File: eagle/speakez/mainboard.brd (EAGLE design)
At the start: 31 parts, among them U1 +12v

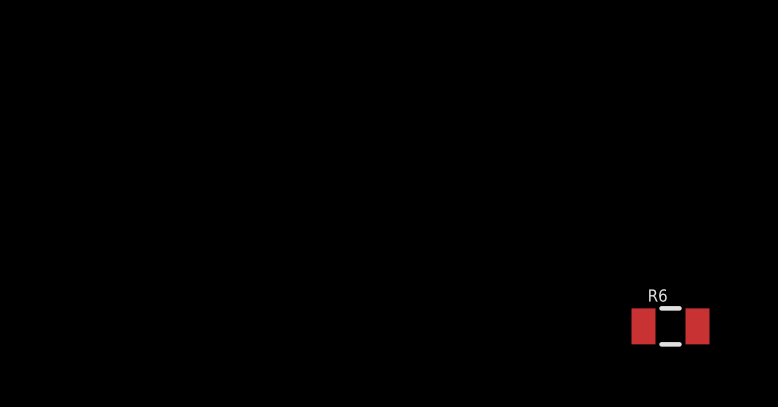
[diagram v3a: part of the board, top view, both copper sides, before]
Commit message: added decoupling caps
to microcontroller VCC pin
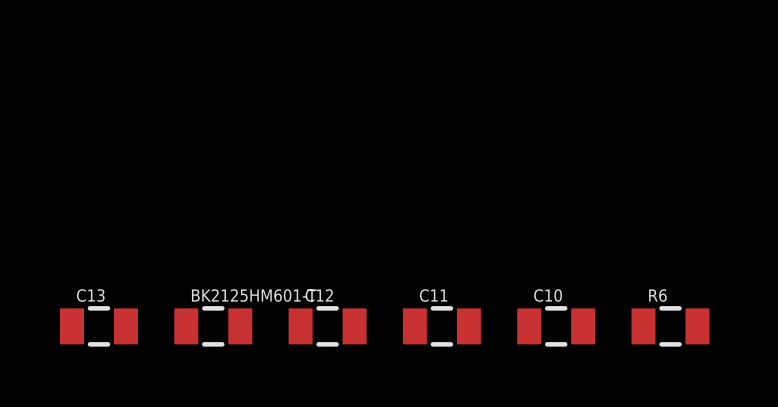
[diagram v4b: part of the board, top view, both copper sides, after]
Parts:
- added BK2125HM601-T: (no value), SparkFun-Passives:0805
- added C10, C11, C12: 0.1uF, SparkFun-Capacitors:0805
- added C13: 2.2uF, SparkFun-Capacitors:0805
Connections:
- removed net N$29: BATTERY.2, C6.2, C7.2, C8.2, PROGRAMMER-RB.1, PROGRAMMER-RB.2, PROGRAMMER-RB.3, PROGRAMMER-RB.4, PROGRAMMER-RB.5, PROGRAMMER-RT.2, PROGRAMMER-RT.3, PROGRAMMER-RT.4, PROGRAMMER-RT.5, SERIAL.4, U$1.31, U$1.4, U$1.47, U1.3
- new net N$22: BATTERY.2, C10.2, C11.2, C12.2, C13.2, C6.2, C7.2, C8.2, PROGRAMMER-RB.1, PROGRAMMER-RB.2, PROGRAMMER-RB.3, PROGRAMMER-RB.4, PROGRAMMER-RB.5, PROGRAMMER-RT.2, PROGRAMMER-RT.3, PROGRAMMER-RT.4, PROGRAMMER-RT.5, SERIAL.4, U$1.31, U$1.4, U$1.47, U1.3
- net N$16: now also C10.1, C11.1, C12.1, C13.1
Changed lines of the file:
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@@
 <element name="PROGRAMMER-RB" library="pel_hdr" package="PH005-1-5" value="PH1X5-05" x="-63.5" y="-163.83"/>
 <element name="R6" library="SparkFun-Passives" package="0805" value="100k" x="-72.39" y="-167.64"/>
+<element name="C10" library="SparkFun-Capacitors" package="0805" value="0.1uF" x="-76.2" y="-167.64"/>
+<element name="C11" library="SparkFun-Capacitors" package="0805" value="0.1uF" x="-80.01" y="-167.64"/>
+<element name="C12" library="SparkFun-Capacitors" package="0805" value="0.1uF" x="-83.82" y="-167.64"/>
+<element name="BK2125HM601-T" library="SparkFun-Passives" package="0805" value="" x="-87.63" y="-167.64"/>
+<element name="C13" library="SparkFun-Capacitors" package="0805" value="2.2uF" x="-91.44" y="-167.64"/>
 </elements>
 <signals>
@@
 <contactref element="PROGRAMMER-LT" pad="1"/>
 <contactref element="R6" pad="1"/>
+<contactref element="C10" pad="1"/>
+<contactref element="C11" pad="1"/>
+<contactref element="C12" pad="1"/>
+<contactref element="C13" pad="1"/>
+<wire x1="-80.91" y1="-167.64" x2="-84.72" y2="-167.64" width="0" layer="19" extent="1-1"/>
+<wire x1="-77.1" y1="-167.64" x2="-80.91" y2="-167.64" width="0" layer="19" extent="1-1"/>
+<wire x1="-73.29" y1="-167.64" x2="-77.1" y2="-167.64" width="0" layer="19" extent="1-1"/>
+<wire x1="-92.34" y1="-167.64" x2="-84.72" y2="-167.64" width="0" layer="19" extent="1-1"/>
 <wire x1="-62.23" y1="-124.46" x2="-73.29" y2="-167.64" width="0" layer="19" extent="1-1"/>
 <wire x1="-49.53" y1="-109.22" x2="-62.23" y2="-124.46" width="0" layer="19" extent="1-1"/>
@@
 <wire x1="58.42" y1="46.99" x2="-63.87" y2="-114.3" width="0" layer="19" extent="1-1"/>
 </signal>
-<signal name="N$29">
+<signal name="N$14">
+<contactref element="U$1" pad="22"/>
+<contactref element="PROGRAMMER-LT" pad="5"/>
+<wire x1="-21.5646" y1="-20.955" x2="-50.8" y2="-95.25" width="0" layer="19" extent="1-1"/>
+</signal>
+<signal name="N$21">
+<contactref element="U$1" pad="23"/>
+<contactref element="PROGRAMMER-LB" pad="4"/>
+<wire x1="-21.082" y1="-20.955" x2="-59.69" y2="-138.43" width="0" layer="19" extent="1-1"/>
+</signal>
+<signal name="N$22">
+<contactref element="C11" pad="2"/>
+<contactref element="C12" pad="2"/>
 <contactref element="PROGRAMMER-RT" pad="2"/>
 <contactref element="PROGRAMMER-RT" pad="3"/>
@@
 <contactref element="C8" pad="2"/>
 <contactref element="SERIAL" pad="4"/>
+<contactref element="C10" pad="2"/>
+<contactref element="C13" pad="2"/>
+<wire x1="-79.11" y1="-167.64" x2="-82.92" y2="-167.64" width="0" layer="19" extent="1-1"/>
+<wire x1="-75.3" y1="-167.64" x2="-79.11" y2="-167.64" width="0" layer="19" extent="1-1"/>
+<wire x1="-90.54" y1="-167.64" x2="-82.92" y2="-167.64" width="0" layer="19" extent="1-1"/>
+<wire x1="-63.5" y1="-163.83" x2="-75.3" y2="-167.64" width="0" layer="19" extent="1-1"/>
 <wire x1="-62.23" y1="-163.83" x2="-63.5" y2="-163.83" width="0" layer="19" extent="1-1"/>
 <wire x1="-60.96" y1="-163.83" x2="-62.23" y2="-163.83" width="0" layer="19" extent="1-1"/>
@@
 <wire x1="75.2" y1="43.18" x2="-14.605" y2="-11.9888" width="0" layer="19" extent="1-1"/>
 </signal>
-<signal name="N$14">
-<contactref element="U$1" pad="22"/>
-<contactref element="PROGRAMMER-LT" pad="5"/>
-<wire x1="-21.5646" y1="-20.955" x2="-50.8" y2="-95.25" width="0" layer="19" extent="1-1"/>
-</signal>
-<signal name="N$21">
-<contactref element="U$1" pad="23"/>
-<contactref element="PROGRAMMER-LB" pad="4"/>
-<wire x1="-21.082" y1="-20.955" x2="-59.69" y2="-138.43" width="0" layer="19" extent="1-1"/>
-</signal>
 </signals>

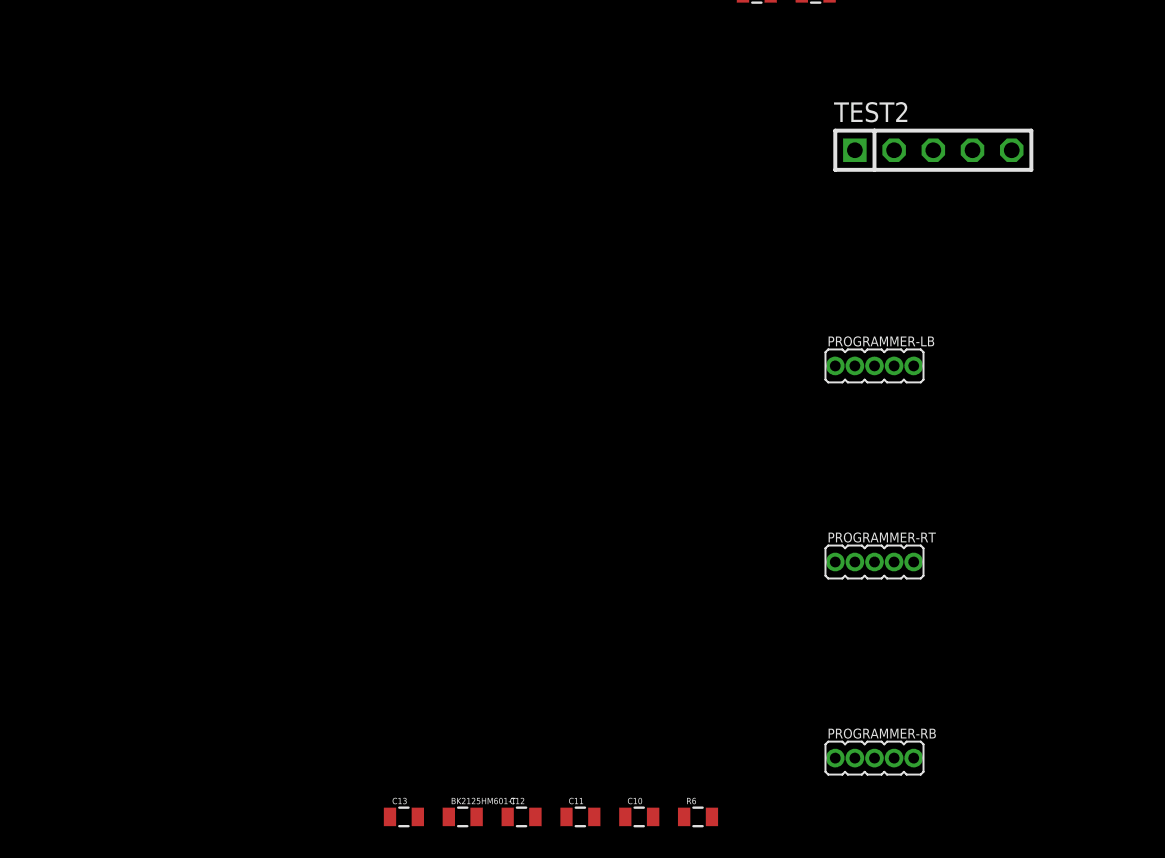
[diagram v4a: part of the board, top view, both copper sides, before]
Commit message: finished copying over Teensy schematic
Added a few more caps and ferrite beads to the microcontroller pins. I
didn't connect VREF-H directly to VBAT. Added test pins.
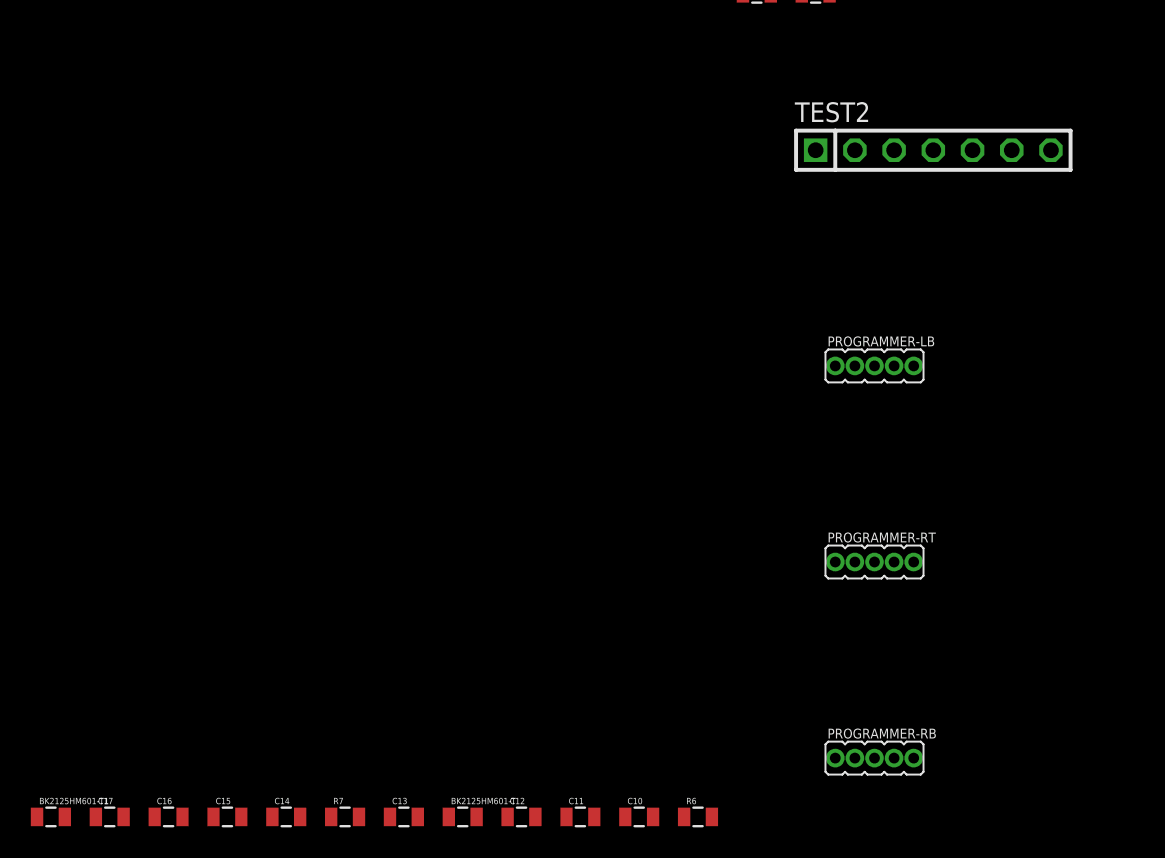
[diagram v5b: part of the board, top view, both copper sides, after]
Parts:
- added BK2125HM601-T1: (no value), SparkFun-Passives:0805
- added C14, C15, C16: 0.1uF, SparkFun-Capacitors:0805
- added C17: 2.2uF, SparkFun-Capacitors:0805
- added R7: 470, SparkFun-Passives:0805
- TEST2: device pinhead:1X05 -> pinhead:1X07
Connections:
- removed net N$16: C10.1, C11.1, C12.1, C13.1, C4.2, C6.1, C8.1, PROGRAMMER-LT.1, R4.1, R6.1, SERIAL.3, TEST2.1, U$1.3, U$1.30, U$1.48, U1.2, VOICE.4
- new net N$29: BK2125HM601-T1.1, C15.2, C16.2, C17.2, TEST2.5, U$1.15, U$1.16
- new net N$30: BK2125HM601-T.2, C17.1, R7.2, TEST2.3, U$1.13
- new net N$31: C15.1, U$1.17
- net GND: now also BATTERY.2, BK2125HM601-T1.2, C10.2, C11.2, C12.2, C13.2, C14.2, C6.2, C7.2, C8.2, PROGRAMMER-RB.1, PROGRAMMER-RB.2, PROGRAMMER-RB.3, PROGRAMMER-RB.4, PROGRAMMER-RB.5, PROGRAMMER-RT.2, PROGRAMMER-RT.3, PROGRAMMER-RT.4, PROGRAMMER-RT.5, SERIAL.4, U$1.31, U$1.4, U$1.47, U1.3
- net N$22: now also C16.1, R7.1, TEST2.4, U$1.14; no longer BATTERY.2, C10.2, C11.2, C12.2, C13.2, C6.2, C7.2, C8.2, PROGRAMMER-RB.1, PROGRAMMER-RB.2, PROGRAMMER-RB.3, PROGRAMMER-RB.4, PROGRAMMER-RB.5, PROGRAMMER-RT.2, PROGRAMMER-RT.3, PROGRAMMER-RT.4, PROGRAMMER-RT.5, SERIAL.4, U$1.31, U$1.4, U$1.47, U1.3
- net N$3: now also BK2125HM601-T.1, C10.1, C11.1, C12.1, C13.1, C14.1, C4.2, C6.1, C8.1, PROGRAMMER-LT.1, R4.1, R6.1, SERIAL.3, TEST2.1, TEST2.6, TEST2.7, U$1.3, U$1.30, U$1.48, U1.2, VOICE.4; no longer U$1.14
